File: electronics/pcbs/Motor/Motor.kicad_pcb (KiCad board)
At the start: 2 copper layers, 86.5 x 53.3 mm, 17 parts, among them J1 Left Encoder, J2 Right Encoder, J3 Battery, J4 I2C, P1 Digital, P10 CONN_01X01, P11 CONN_01X01, P12 CONN_01X01, P13 CONN_01X01, P2 Power, P3 Analog, P4 Analog, P5 PWM, P6 PWM, P7 Communication, P9 CONN_01X01

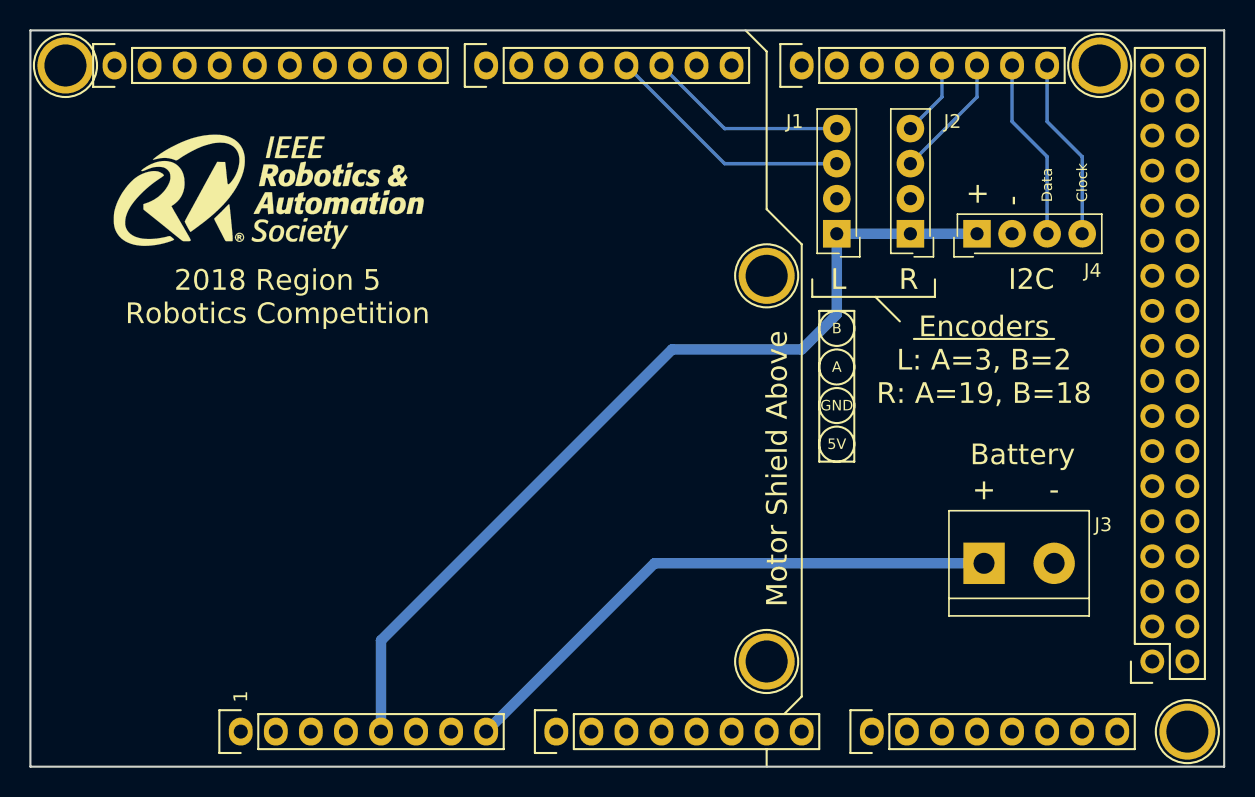
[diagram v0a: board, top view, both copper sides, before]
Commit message: Motor PCB: Modified PCB to be more easily printed with labels on the OtherMill.
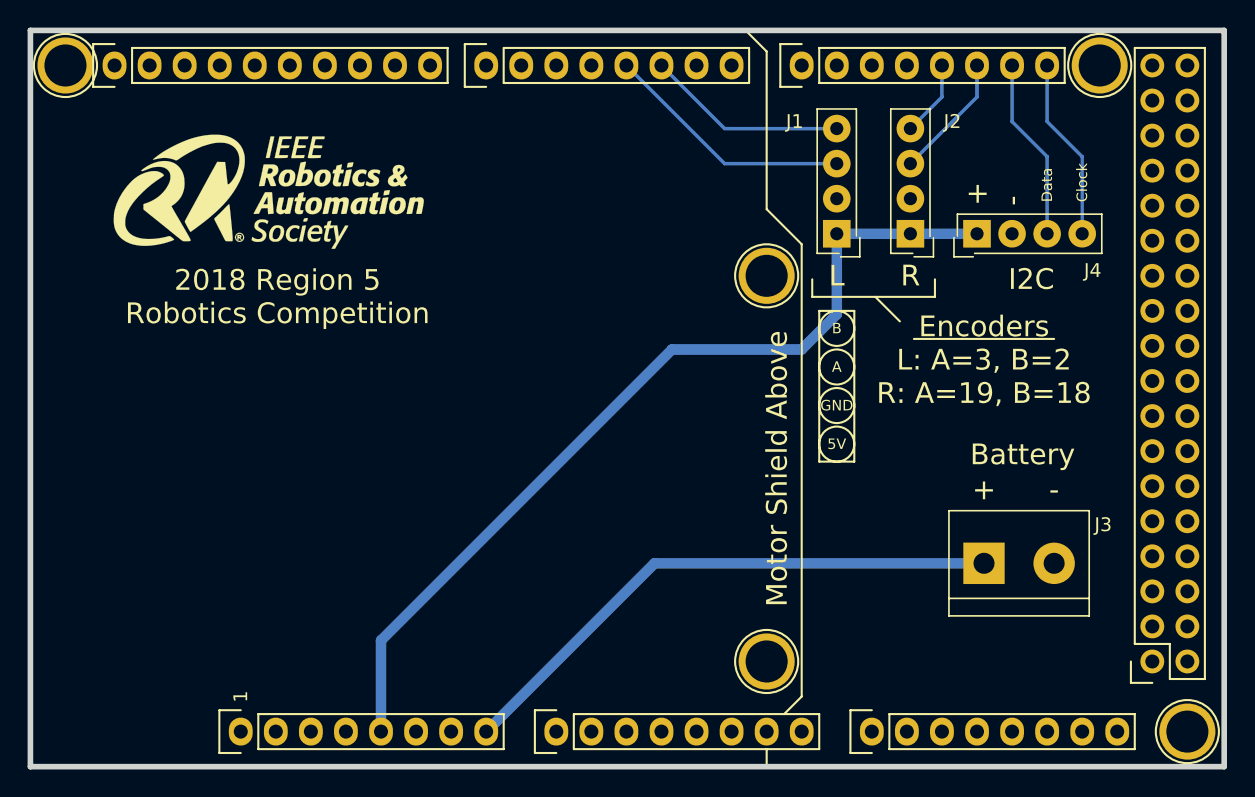
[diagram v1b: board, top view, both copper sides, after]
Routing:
- added copper zone on F.Cu, net GND
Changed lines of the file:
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@@
     (area 96.952999 66.843 204.931334 122.995)
     (thickness 1.6)
-    (drawings 64)
+    (drawings 89)
     (tracks 23)
     (zones 0)
@@
     (35 F.Paste user)
     (36 B.SilkS user)
-    (37 F.SilkS user)
+    (37 F.SilkS user hide)
     (38 B.Mask user)
     (39 F.Mask user)
@@
     (45 Margin user)
     (46 B.CrtYd user)
-    (47 F.CrtYd user)
+    (47 F.CrtYd user hide)
     (48 B.Fab user)
     (49 F.Fab user hide)
@@
     (zone_45_only no)
     (trace_min 0.2)
-    (segment_width 0.15)
-    (edge_width 0.15)
+    (segment_width 0.4064)
+    (edge_width 0.4064)
     (via_size 0.6)
     (via_drill 0.4)
@@
       (xy -2.277533 3.132666) (xy -2.182283 3.132713)) (layer F.SilkS) (width 0.01))
   )
-  (gr_line (start 202.565 68.326) (end 202.565 121.666) (angle 90) (layer Edge.Cuts) (width 0.15))
+  (gr_line (start 173.228 99.822) (end 173.228 88.138) (angle 90) (layer Cmts.User) (width 0.4064))
+  (gr_line (start 175.768 99.822) (end 173.228 99.822) (angle 90) (layer Cmts.User) (width 0.4064))
+  (gr_line (start 175.768 88.138) (end 175.768 99.822) (angle 90) (layer Cmts.User) (width 0.4064))
+  (gr_line (start 173.228 88.138) (end 175.768 88.138) (angle 90) (layer Cmts.User) (width 0.4064))
+  (gr_text - (at 190.246 101.6) (layer F.SilkS)
+    (effects (font (size 1.5 1.5) (thickness 0.3)))
+  )
+  (gr_text + (at 185.166 101.6) (layer Cmts.User)
+    (effects (font (size 1.651 1.651) (thickness 0.4064)))
+  )
+  (gr_text Battery (at 187.96 99.06) (layer Cmts.User)
+    (effects (font (size 1.651 1.651) (thickness 0.4064)))
+  )
+  (gr_text Clock (at 192.278 80.772 90) (layer Cmts.User)
+    (effects (font (size 1.651 1.651) (thickness 0.4064)) (justify left))
+  )
+  (gr_text Data (at 189.738 80.772 90) (layer Cmts.User)
+    (effects (font (size 1.651 1.651) (thickness 0.4064)) (justify left))
+  )
+  (gr_text - (at 187.198 81.026 90) (layer Cmts.User)
+    (effects (font (size 1.651 1.651) (thickness 0.4064)) (justify left))
+  )
+  (gr_text + (at 184.658 81.026 90) (layer Cmts.User)
+    (effects (font (size 1.651 1.651) (thickness 0.4064)) (justify left))
+  )
+  (gr_text I2C (at 188.722 86.36) (layer Cmts.User)
+    (effects (font (size 1.651 1.651) (thickness 0.4064)))
+  )
+  (gr_text "Encoders\nL: A=3, B=2\nR: A=19, B=18" (at 185.928 92.202) (layer Cmts.User)
+    (effects (font (size 1.651 1.651) (thickness 0.4064)))
+  )
+  (gr_line (start 169.418 69.85) (end 167.894 68.326) (angle 90) (layer Cmts.User) (width 0.4064))
+  (gr_line (start 169.418 81.28) (end 169.418 69.85) (angle 90) (layer Cmts.User) (width 0.4064))
+  (gr_line (start 171.958 83.82) (end 169.418 81.28) (angle 90) (layer Cmts.User) (width 0.4064))
+  (gr_line (start 171.958 116.586) (end 171.958 83.82) (angle 90) (layer Cmts.User) (width 0.4064))
+  (gr_text "Motor Shield\nAbove" (at 168.91 99.568 90) (layer Cmts.User)
+    (effects (font (size 1.651 1.651) (thickness 0.4064)))
+  )
+  (gr_text + (at 174.498 98.298) (layer Cmts.User)
+    (effects (font (size 1.651 1.651) (thickness 0.4064)))
+  )
+  (gr_text - (at 174.498 95.504) (layer Cmts.User)
+    (effects (font (size 1.651 1.651) (thickness 0.4064)))
+  )
+  (gr_text A (at 174.498 92.71) (layer Cmts.User)
+    (effects (font (size 1.651 1.651) (thickness 0.4064)))
+  )
+  (gr_text B (at 174.498 89.916) (layer F.SilkS)
+    (effects (font (size 0.762 0.762) (thickness 0.1905)))
+  )
+  (gr_text R (at 179.832 86.106) (layer F.SilkS)
+    (effects (font (size 1.5 1.5) (thickness 0.3)))
+  )
+  (gr_text L (at 174.498 86.106) (layer F.SilkS)
+    (effects (font (size 1.5 1.5) (thickness 0.3)))
+  )
+  (gr_text "2018 Region 5\nRobotics Competition" (at 133.985 87.63) (layer Cmts.User)
+    (effects (font (size 1.651 1.651) (thickness 0.4064)))
+  )
+  (gr_line (start 202.565 68.326) (end 202.565 121.666) (angle 90) (layer Edge.Cuts) (width 0.4064))
   (gr_text "2018 Region 5\nRobotics Competition" (at 133.985 87.63) (layer F.SilkS)
     (effects (font (size 1.5 1.5) (thickness 0.3)))
@@
     (effects (font (size 1.5 1.5) (thickness 0.3)))
   )
-  (gr_text - (at 190.246 101.6) (layer F.SilkS)
-    (effects (font (size 1.5 1.5) (thickness 0.3)))
+  (gr_text - (at 190.246 101.6) (layer Cmts.User)
+    (effects (font (size 1.651 1.651) (thickness 0.4064)))
   )
   (gr_text + (at 185.166 101.6) (layer F.SilkS)
@@
     (effects (font (size 1.5 1.5) (thickness 0.3)))
   )
-  (gr_text R (at 179.705 86.36) (layer F.SilkS)
-    (effects (font (size 1.5 1.5) (thickness 0.3)))
-  )
-  (gr_text L (at 174.625 86.36) (layer F.SilkS)
-    (effects (font (size 1.5 1.5) (thickness 0.3)))
+  (gr_text R (at 179.832 86.106) (layer Cmts.User)
+    (effects (font (size 1.651 1.651) (thickness 0.4064)))
+  )
+  (gr_text L (at 174.498 86.106) (layer Cmts.User)
+    (effects (font (size 1.651 1.651) (thickness 0.4064)))
   )
   (gr_line (start 181.61 87.63) (end 181.61 86.36) (angle 90) (layer F.SilkS) (width 0.15))
@@
     (effects (font (size 0.762 0.762) (thickness 0.1905)))
   )
-  (gr_text B (at 174.498 89.916) (layer F.SilkS)
-    (effects (font (size 0.762 0.762) (thickness 0.1905)))
+  (gr_text B (at 174.498 89.916) (layer Cmts.User)
+    (effects (font (size 1.651 1.651) (thickness 0.4064)))
   )
   (gr_text GND (at 174.498 95.504) (layer F.SilkS)
@@
   (gr_line (start 114.808 109.601) (end 114.808 118.491) (angle 90) (layer Dwgs.User) (width 0.15))
   (gr_line (start 101.473 109.601) (end 114.808 109.601) (angle 90) (layer Dwgs.User) (width 0.15))
-  (gr_line (start 202.565 121.666) (end 116.078 121.666) (angle 90) (layer Edge.Cuts) (width 0.15))
-  (gr_line (start 116.078 68.326) (end 202.565 68.326) (angle 90) (layer Edge.Cuts) (width 0.15))
-  (gr_line (start 116.078 121.666) (end 116.078 68.326) (angle 90) (layer Edge.Cuts) (width 0.15))
+  (gr_line (start 202.565 121.666) (end 116.078 121.666) (angle 90) (layer Edge.Cuts) (width 0.4064))
+  (gr_line (start 116.078 68.326) (end 202.565 68.326) (angle 90) (layer Edge.Cuts) (width 0.4064))
+  (gr_line (start 116.078 121.666) (end 116.078 68.326) (angle 90) (layer Edge.Cuts) (width 0.4064))
   (segment (start 174.498 83.058) (end 174.498 88.9) (width 0.762) (layer B.Cu) (net 34))
   (segment (start 141.478 112.522) (end 141.478 119.126) (width 0.762) (layer B.Cu) (net 34))
@@
     (connect_pads (clearance 0.508))
     (min_thickness 0.254)
+    (fill yes (arc_segments 16) (thermal_gap 0.508) (thermal_bridge_width 0.508))
+    (polygon
+      (pts
+        (xy 202.565 121.666) (xy 116.078 121.666) (xy 116.078 68.326) (xy 202.565 68.326)
+      )
+    )
+  )
+  (zone (net 1) (net_name GND) (layer F.Cu) (hatch edge 0.508)
+    (connect_pads (clearance 0.508))
+    (min_thickness 0.254)
